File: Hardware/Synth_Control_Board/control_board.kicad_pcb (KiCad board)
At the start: 2 copper layers, 157.5 x 157.5 mm, 100 parts, among them J1 Conn_02x13_Odd_Even, J10 Conn_01x05, J11 Conn_01x08, J2 Conn_01x03, J3 Conn_02x13_Odd_Even, J4 Conn_01x08, J7 Conn_01x05, J8 Conn_01x05, J9 Conn_01x05, SW1 SW_DPDT_x2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

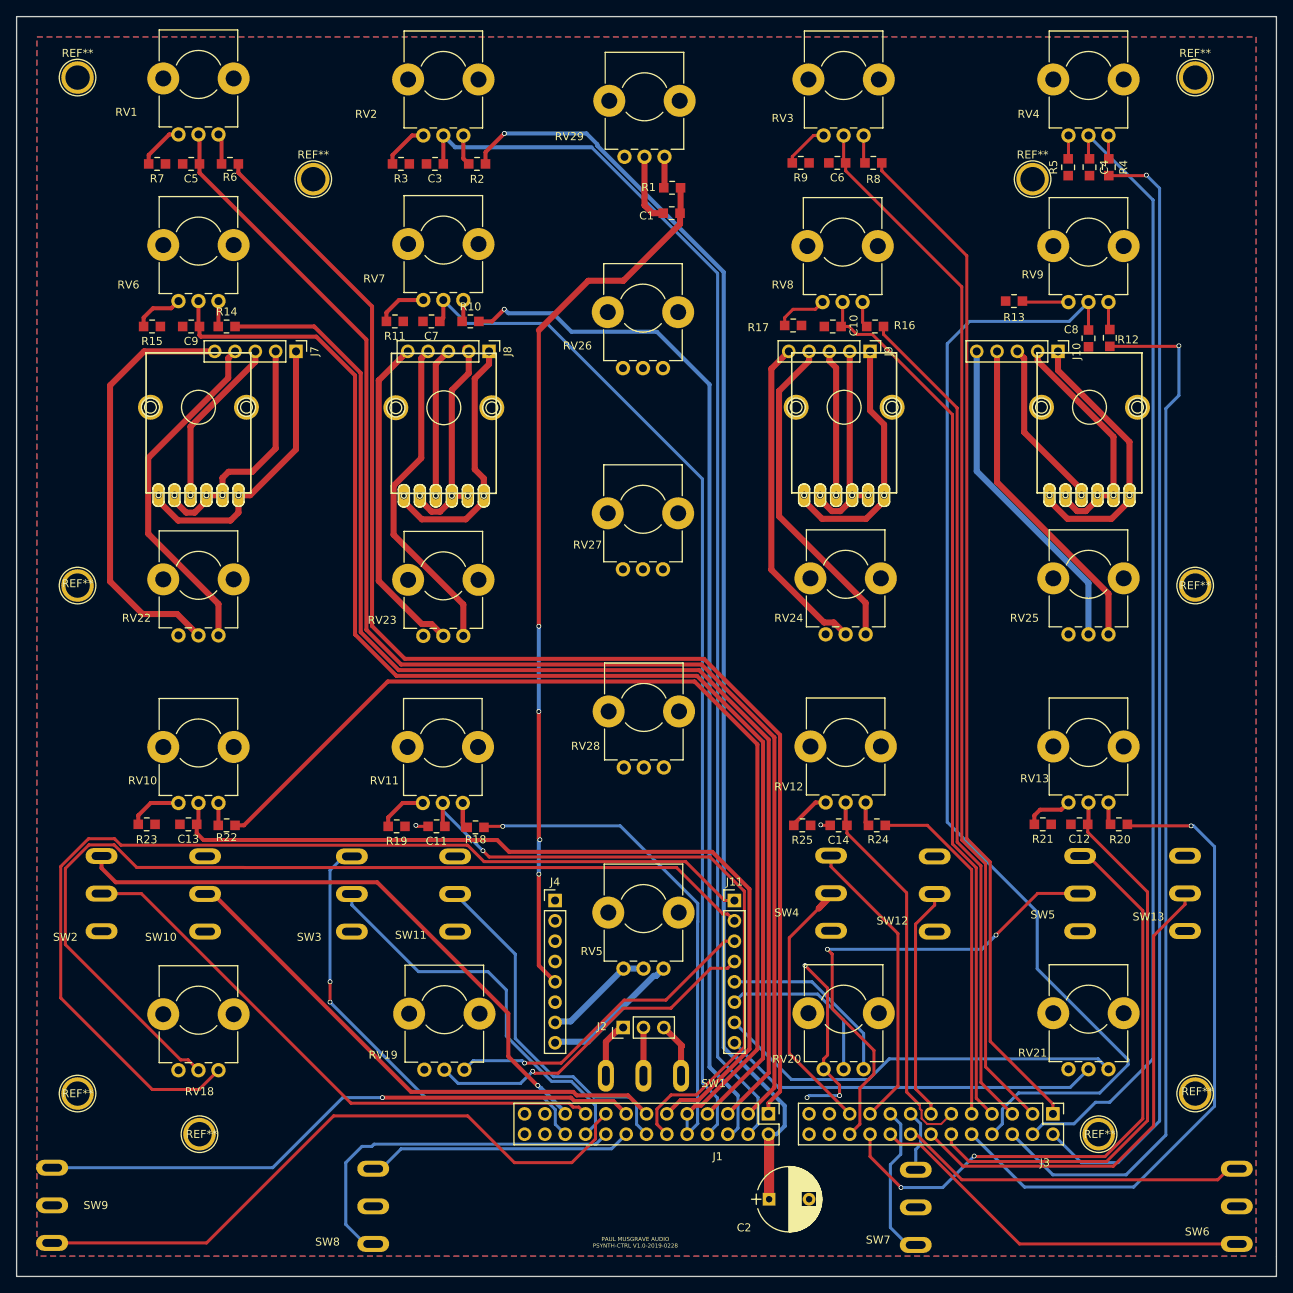
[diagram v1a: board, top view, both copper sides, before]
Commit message: fix backward filter potentiometers
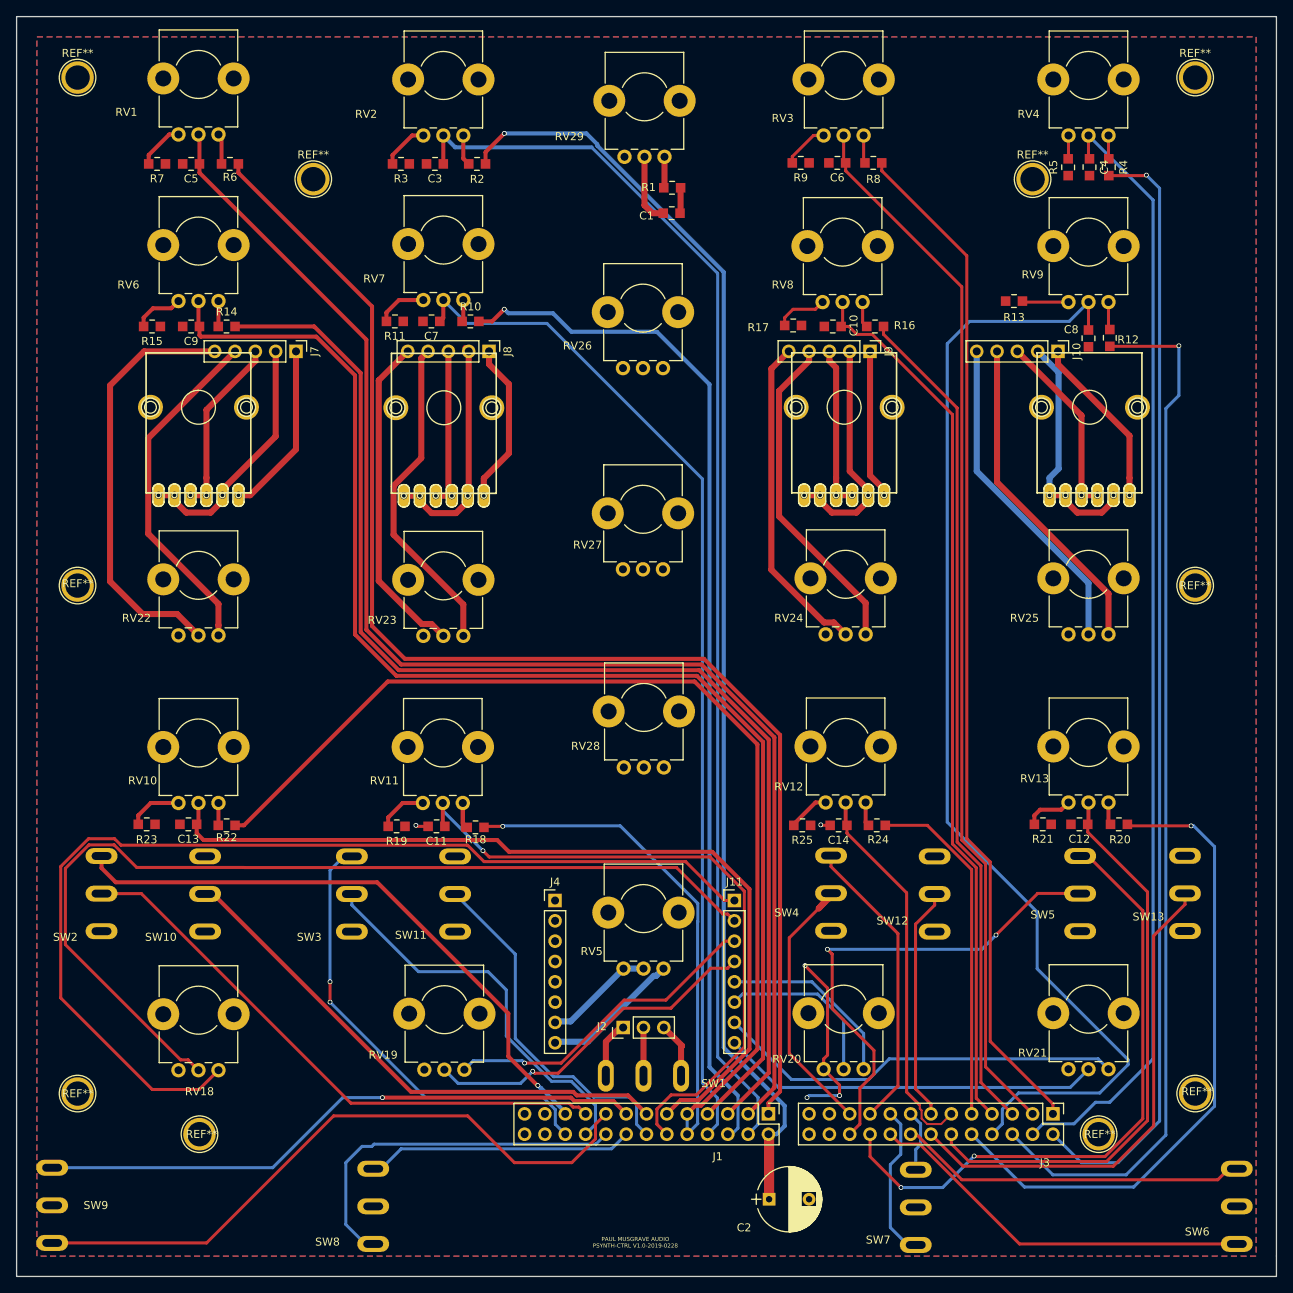
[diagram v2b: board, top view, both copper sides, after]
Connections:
- J4 pad 5: /delay_in -> /delay_mix_in
- J4 pad 6: /delay_out -> /delay_mix_out
- RV14 pad A2: /freq_in_2 -> /freq_fb_2
- RV14 pad B2: /freq_fb_2 -> /freq_out_2
- RV15 pad A2: /freq_in_3 -> /freq_fb_3
- RV15 pad B2: /freq_fb_3 -> /freq_out_3
- RV16 pad A2: /freq_in_4 -> /freq_fb_4
- RV16 pad B2: /freq_fb_4 -> /freq_out_4
- RV17 pad A2: /freq_in_1 -> /freq_fb_1
- RV17 pad B2: /freq_fb_1 -> /freq_out_1
- RV26 pad 1: /delay_in_1 -> /delay_fb_in
- RV26 pad 2: /delay_out_1 -> /delay_fb_out
- RV27 pad 1: /delay_in_2 -> /delay_time_in
- RV27 pad 2: /delay_out_2 -> /delay_time_out
- RV28 pad 1: /delay_in_3 -> /delay_mix_in
- RV28 pad 3: /delay_out_3 -> /delay_mix_out
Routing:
- net /delay_in: track 110.1 -> 3.20 mm, vias 4 -> 0
- net /freq_in_1: track 36.1 -> 21.8 mm
- net /freq_in_4: track 35.0 -> 22.4 mm
- net /freq_in_3: track 32.0 -> 19.4 mm
- net /freq_in_2: track 32.5 -> 21.1 mm
- net /freq_fb_3: track 26.4 -> 30.8 mm
- net /freq_out_4: track 21.3 -> 24.5 mm
- net /freq_out_3: track 18.3 -> 21.3 mm
- net /freq_out_1: track 21.3 -> 24.1 mm
- net /freq_fb_2: track 27.8 -> 30.5 mm
- net /freq_out_2: track 18.7 -> 20.7 mm
- net /freq_fb_4: track 30.4 -> 31.6 mm
